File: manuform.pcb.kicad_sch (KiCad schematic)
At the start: 15 parts, among them J1 Conn_01x05, J2 Conn_01x04, J3 Conn_01x01, J4 Conn_01x01, J5 Conn_01x01, SW1 SW_DIP_x01, SW2 SW_DIP_x01, SW3 SW_DIP_x01, SW4 SW_DIP_x01, SW5 SW_DIP_x01

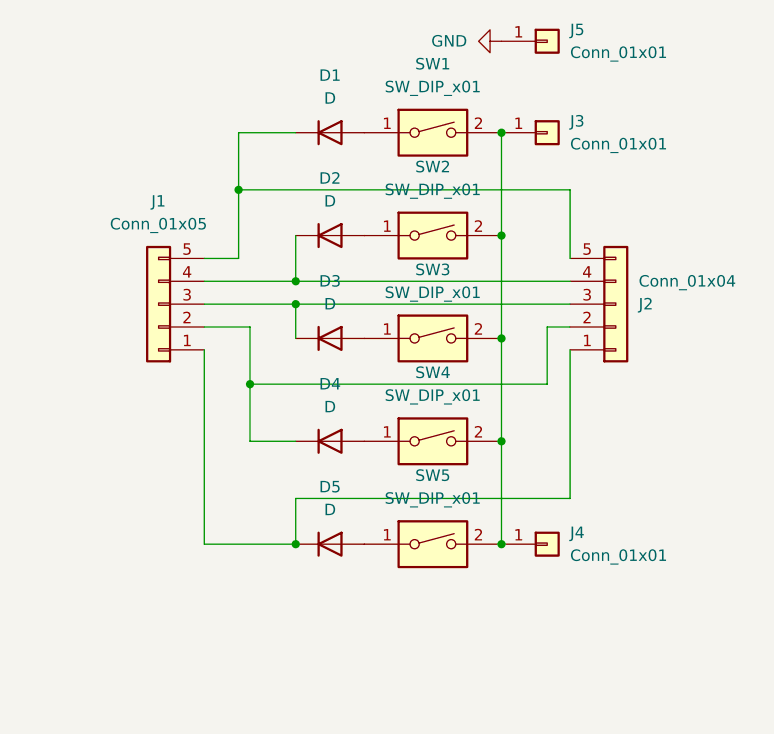
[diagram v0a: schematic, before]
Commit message: increased separation to 25mm
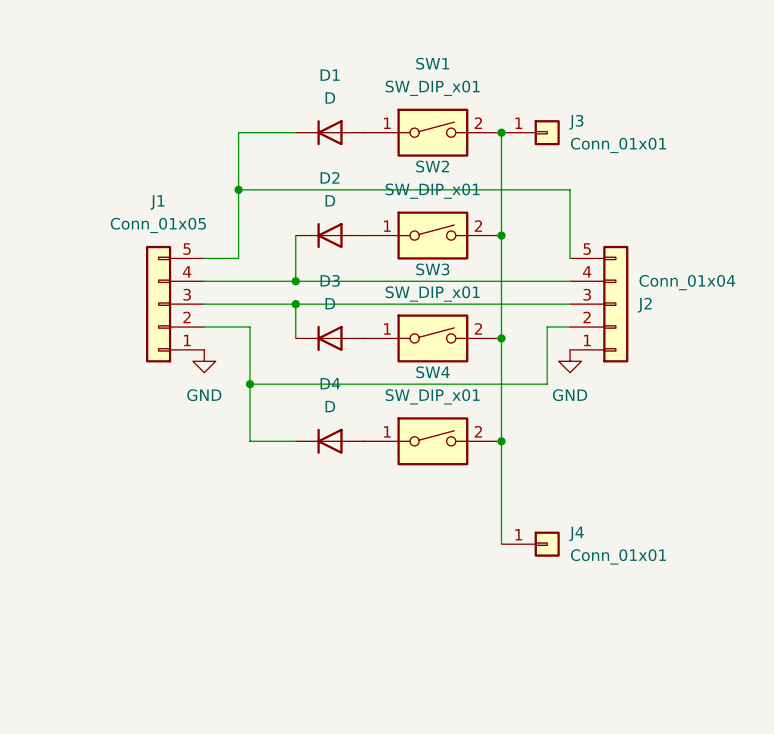
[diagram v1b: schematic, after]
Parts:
- removed D5: D, Diode_SMD:D_0603_1608Metric, symbol Device:D
- removed J5: Conn_01x01, Connector_PinHeader_2.54mm:PinHeader_1x01_P2.54mm_Vertical, symbol Connector_Generic:Conn_01x01
- removed SW5: SW_DIP_x01, Button_Switch_Keyboard:SW_Cherry_MX_1.00u_PCB, symbol Switch:SW_DIP_x01
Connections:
- net GND: now also J1.1 (Pin_1), J2.1 (Pin_1)
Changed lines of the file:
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@@
   (junction (at 119.38 64.77) (diameter 0) (color 0 0 0 0)
   )
-  (junction (at 119.38 99.06) (diameter 0) (color 0 0 0 0)
-  )
   (junction (at 96.52 69.85) (diameter 0) (color 0 0 0 0)
   )
-  (junction (at 96.52 99.06) (diameter 0) (color 0 0 0 0)
-  )
   (junction (at 96.52 72.39) (diameter 0) (color 0 0 0 0)
   )
@@
     (stroke (width 0) (type default))
   )
-  (wire (pts (xy 96.52 99.06) (xy 96.52 93.98))
-    (stroke (width 0) (type default))
-  )
   (wire (pts (xy 86.36 74.93) (xy 91.44 74.93))
     (stroke (width 0) (type default))
   )
-  (wire (pts (xy 86.36 77.47) (xy 86.36 99.06))
-    (stroke (width 0) (type default))
-  )
   (wire (pts (xy 96.52 72.39) (xy 127 72.39))
     (stroke (width 0) (type default))
@@
     (stroke (width 0) (type default))
   )
-  (wire (pts (xy 86.36 99.06) (xy 96.52 99.06))
-    (stroke (width 0) (type default))
-  )
   (wire (pts (xy 127 59.69) (xy 127 67.31))
     (stroke (width 0) (type default))
@@
     (stroke (width 0) (type default))
   )
-  (wire (pts (xy 127 93.98) (xy 127 77.47))
-    (stroke (width 0) (type default))
-  )
   (wire (pts (xy 119.38 64.77) (xy 119.38 76.2))
-    (stroke (width 0) (type default))
-  )
-  (wire (pts (xy 96.52 93.98) (xy 127 93.98))
     (stroke (width 0) (type default))
   )
@@
     )
   )
+  (symbol (lib_id "power:GND") (at 86.36 77.47 0) (unit 1)
+    (in_bom yes) (on_board yes) (dnp no) (fields_autoplaced)
+    (property "Reference" "#PWR02" (at 86.36 83.82 0)
+      (effects (font (size 1.27 1.27)) hide)
+    )
+    (property "Value" "GND" (at 86.36 82.55 0)
+      (effects (font (size 1.27 1.27)))
+    )
+    (property "Footprint" "" (at 86.36 77.47 0)
+      (effects (font (size 1.27 1.27)) hide)
+    )
+    (property "Datasheet" "" (at 86.36 77.47 0)
+      (effects (font (size 1.27 1.27)) hide)
+    )
+    (pin "1")
+    (instances
+      (project "manuform.pcb"
+        (path "/a99954bf-03b6-406e-8be0-527a2c713975"
+          (reference "#PWR02") (unit 1)
+        )
+      )
+    )
+  )
   (symbol (lib_id "Switch:SW_DIP_x01") (at 111.76 53.34 0) (unit 1)
     (in_bom yes) (on_board yes) (dnp no) (fields_autoplaced)
@@
         (path "/a99954bf-03b6-406e-8be0-527a2c713975"
           (reference "SW1") (unit 1)
-        )
-      )
-    )
-  )
-  (symbol (lib_id "Connector_Generic:Conn_01x01") (at 124.46 43.18 0) (unit 1)
-    (in_bom yes) (on_board yes) (dnp no) (fields_autoplaced)
-    (property "Reference" "J5" (at 127 41.91 0)
-      (effects (font (size 1.27 1.27)) (justify left))
-    )
-    (property "Value" "Conn_01x01" (at 127 44.45 0)
-      (effects (font (size 1.27 1.27)) (justify left))
-    )
-    (property "Footprint" "Connector_PinHeader_2.54mm:PinHeader_1x01_P2.54mm_Vertical" (at 124.46 43.18 0)
-      (effects (font (size 1.27 1.27)) hide)
-    )
-    (property "Datasheet" "~" (at 124.46 43.18 0)
-      (effects (font (size 1.27 1.27)) hide)
-    )
-    (pin "1")
-    (instances
-      (project "manuform.pcb"
-        (path "/a99954bf-03b6-406e-8be0-527a2c713975"
-          (reference "J5") (unit 1)
-        )
-      )
-    )
-  )
-  (symbol (lib_id "Device:D") (at 100.33 99.06 0) (unit 1)
-    (in_bom yes) (on_board yes) (dnp no) (fields_autoplaced)
-    (property "Reference" "D5" (at 100.33 92.71 0)
-      (effects (font (size 1.27 1.27)))
-    )
-    (property "Value" "D" (at 100.33 95.25 0)
-      (effects (font (size 1.27 1.27)))
-    )
-    (property "Footprint" "Diode_SMD:D_0603_1608Metric" (at 100.33 99.06 0)
-      (effects (font (size 1.27 1.27)) hide)
-    )
-    (property "Datasheet" "~" (at 100.33 99.06 0)
-      (effects (font (size 1.27 1.27)) hide)
-    )
-    (property "Sim.Device" "D" (at 100.33 99.06 0)
-      (effects (font (size 1.27 1.27)) hide)
-    )
-    (property "Sim.Pins" "1=K 2=A" (at 100.33 99.06 0)
-      (effects (font (size 1.27 1.27)) hide)
-    )
-    (pin "2")
-    (pin "1")
-    (instances
-      (project "manuform.pcb"
-        (path "/a99954bf-03b6-406e-8be0-527a2c713975"
-          (reference "D5") (unit 1)
-        )
-      )
-    )
-  )
-  (symbol (lib_id "Switch:SW_DIP_x01") (at 111.76 99.06 0) (unit 1)
-    (in_bom yes) (on_board yes) (dnp no) (fields_autoplaced)
-    (property "Reference" "SW5" (at 111.76 91.44 0)
-      (effects (font (size 1.27 1.27)))
-    )
-    (property "Value" "SW_DIP_x01" (at 111.76 93.98 0)
-      (effects (font (size 1.27 1.27)))
-    )
-    (property "Footprint" "Button_Switch_Keyboard:SW_Cherry_MX_1.00u_PCB" (at 111.76 99.06 0)
-      (effects (font (size 1.27 1.27)) hide)
-    )
-    (property "Datasheet" "~" (at 111.76 99.06 0)
-      (effects (font (size 1.27 1.27)) hide)
-    )
-    (pin "1")
-    (pin "2")
-    (instances
-      (project "manuform.pcb"
-        (path "/a99954bf-03b6-406e-8be0-527a2c713975"
-          (reference "SW5") (unit 1)
         )
       )
@@
     )
   )
-  (symbol (lib_id "power:GND") (at 119.38 43.18 270) (unit 1)
-    (in_bom yes) (on_board yes) (dnp no) (fields_autoplaced)
-    (property "Reference" "#PWR01" (at 113.03 43.18 0)
-      (effects (font (size 1.27 1.27)) hide)
-    )
-    (property "Value" "GND" (at 115.57 43.18 90)
-      (effects (font (size 1.27 1.27)) (justify right))
-    )
-    (property "Footprint" "" (at 119.38 43.18 0)
-      (effects (font (size 1.27 1.27)) hide)
-    )
-    (property "Datasheet" "" (at 119.38 43.18 0)
-      (effects (font (size 1.27 1.27)) hide)
-    )
+  (symbol (lib_id "power:GND") (at 127 77.47 0) (unit 1)
+    (in_bom yes) (on_board yes) (dnp no) (fields_autoplaced)
+    (property "Reference" "#PWR01" (at 127 83.82 0)
+      (effects (font (size 1.27 1.27)) hide)
+    )
+    (property "Value" "GND" (at 127 82.55 0)
+      (effects (font (size 1.27 1.27)))
+    )
+    (property "Footprint" "" (at 127 77.47 0)
+      (effects (font (size 1.27 1.27)) hide)
+    )
+    (property "Datasheet" "" (at 127 77.47 0)
+      (effects (font (size 1.27 1.27)) hide)
+    )

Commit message: reduced the spacing, flipped switch fp horiz
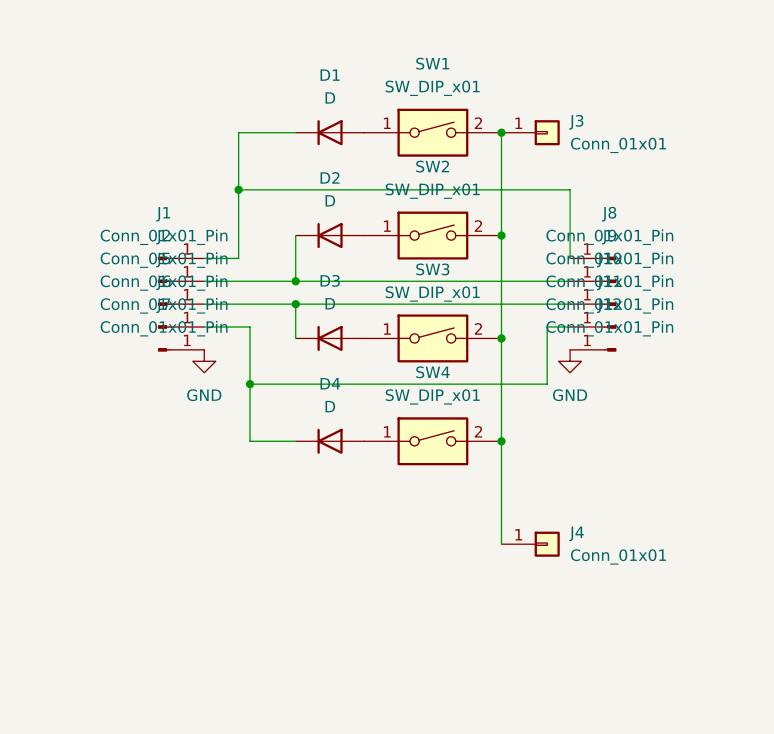
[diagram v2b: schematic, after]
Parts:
- removed J1: Conn_01x05, Connector_PinHeader_2.54mm:PinHeader_1x05_P2.54mm_Vertical, symbol Connector_Generic:Conn_01x05
- removed J2: Conn_01x04, Connector_PinHeader_2.54mm:PinHeader_1x05_P2.54mm_Vertical, symbol Connector_Generic:Conn_01x05
- added J1, J10, J11, J12, J2, J5, J6, J7, J8, J9: Conn_01x01_Pin, Connector_PinHeader_2.54mm:PinHeader_1x01_P2.54mm_Vertical, symbol Connector:Conn_01x01_Pin
- D1, D2, D3, D4: footprint Diode_SMD:D_0603_1608Metric -> Diode_SMD:D_SOD-123
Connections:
- net GND: now also J12.1 (Pin_1), J7.1 (Pin_1)
- net at D4.1 (K): now also J11.1 (Pin_1), J6.1 (Pin_1)
- net at D3.1 (K): now also J10.1 (Pin_1), J5.1 (Pin_1)
- net at D2.1 (K): now also J2.1 (Pin_1), J9.1 (Pin_1)
- net at D1.1 (K): now also J1.1 (Pin_1), J8.1 (Pin_1)

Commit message: new version with longer mehanical and solder holes.
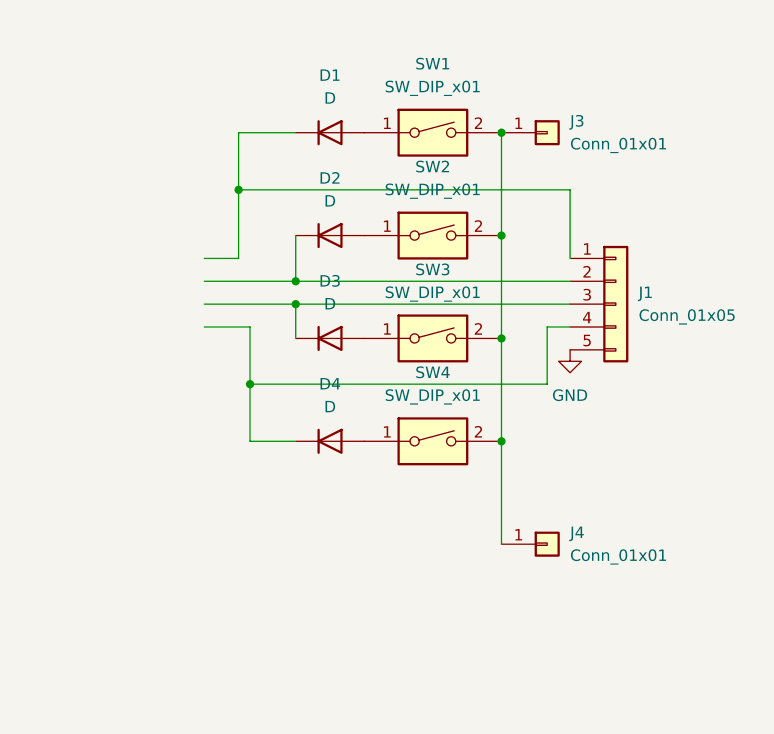
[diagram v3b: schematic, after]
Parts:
- removed J1, J10, J11, J12, J2, J5, J6, J7, J8, J9: Conn_01x01_Pin, Connector_PinHeader_2.54mm:PinHeader_1x01_P2.54mm_Vertical, symbol Connector:Conn_01x01_Pin
- added J1: Conn_01x05, Connector_PinHeader_2.54mm:PinHeader_1x05_P2.54mm_Vertical, symbol Connector_Generic:Conn_01x05
- SW1, SW2, SW3, SW4: footprint Button_Switch_Keyboard:SW_Cherry_MX_1.00u_PCB -> switchCustom:SW_Cherry_MX_1.00u_PCB
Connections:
- net GND: now also J1.5 (Pin_5)
- net at D2.1 (K): now also J1.2 (Pin_2)
- net at D4.1 (K): now also J1.4 (Pin_4)
- net at D3.1 (K): now also J1.3 (Pin_3)
- net at D1.1 (K): now also J1.1 (Pin_1)

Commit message: updated the sch for 6 rows.
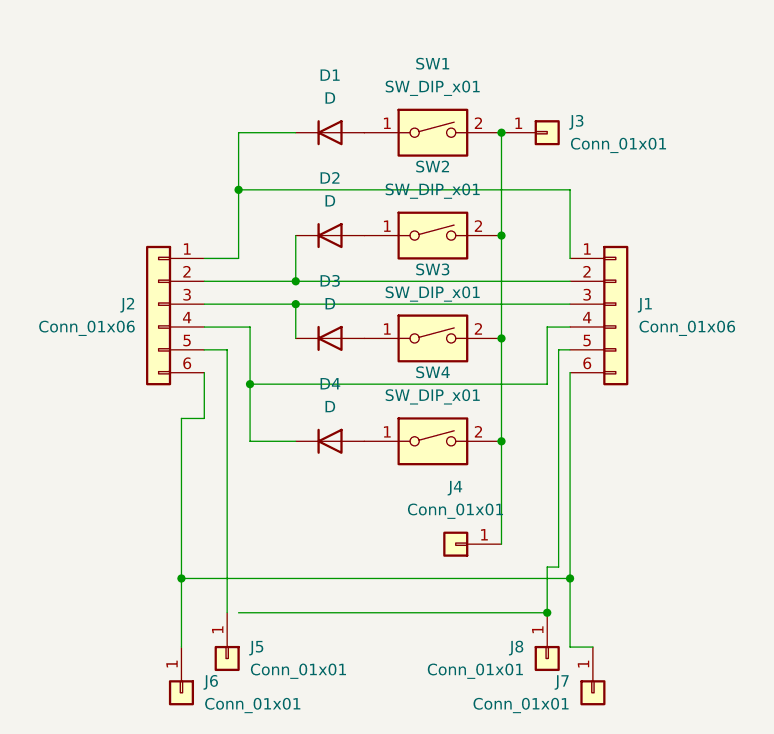
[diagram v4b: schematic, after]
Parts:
- added J2: Conn_01x06, Connector_PinSocket_2.00mm:PinSocket_1x06_P2.00mm_Vertical, symbol Connector_Generic:Conn_01x06
- added J5, J6, J7, J8: Conn_01x01, Connector_PinHeader_2.54mm:PinHeader_1x01_P2.54mm_Vertical, symbol Connector_Generic:Conn_01x01
- D1: footprint Diode_SMD:D_SOD-123 -> Diode_THT:D_DO-35_SOD27_P7.62mm_Horizontal
- J1: value Conn_01x05 -> Conn_01x06; footprint Connector_PinHeader_2.54mm:PinHeader_1x05_P2.54mm_Vertical -> Connector_PinSocket_2.00mm:PinSocket_1x06_P2.00mm_Vertical; symbol Connector_Generic:Conn_01x05 -> Connector_Generic:Conn_01x06
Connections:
- net at D1.1 (K), J1.1 (Pin_1): now also J2.1 (Pin_1)
- net at D3.1 (K), J1.3 (Pin_3): now also J2.3 (Pin_3)
- net at D2.1 (K), J1.2 (Pin_2): now also J2.2 (Pin_2)
- net at D4.1 (K), J1.4 (Pin_4): now also J2.4 (Pin_4)
- net GND: no longer names the net of J1.5 (Pin_5)
- net GND: now also J8.1 (Pin_1)
- new net: J1.6 (Pin_6), J2.6 (Pin_6), J6.1 (Pin_1), J7.1 (Pin_1)
- new net: J2.5 (Pin_5), J5.1 (Pin_1)
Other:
- moved on the sheet: J4

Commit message: 6 rows MX v1.0
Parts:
- D2, D3, D4: footprint Diode_SMD:D_SOD-123 -> Diode_THT:D_DO-35_SOD27_P7.62mm_Horizontal
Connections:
- net at J1.6 (Pin_6), J2.6 (Pin_6), J6.1 (Pin_1): no longer J7.1 (Pin_1)
- net at J2.5 (Pin_5), J5.1 (Pin_1): now also J1.5 (Pin_5)
- net GND: now reaches J8.1 (Pin_1)
- net GND: now also J7.1 (Pin_1); no longer J1.5 (Pin_5)
